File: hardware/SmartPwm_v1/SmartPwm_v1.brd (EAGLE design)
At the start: 100 x 80 mm, 22 parts, among them IC1 7805T, J1 ESP32-PICO-KIT, Q1 IRF3704-H, Q2 IRF3704-H, Q3 IRF3704-H, Q4 IRF3704-H, U1 ICL7667CPAZ, U2 ICL7667CPAZ

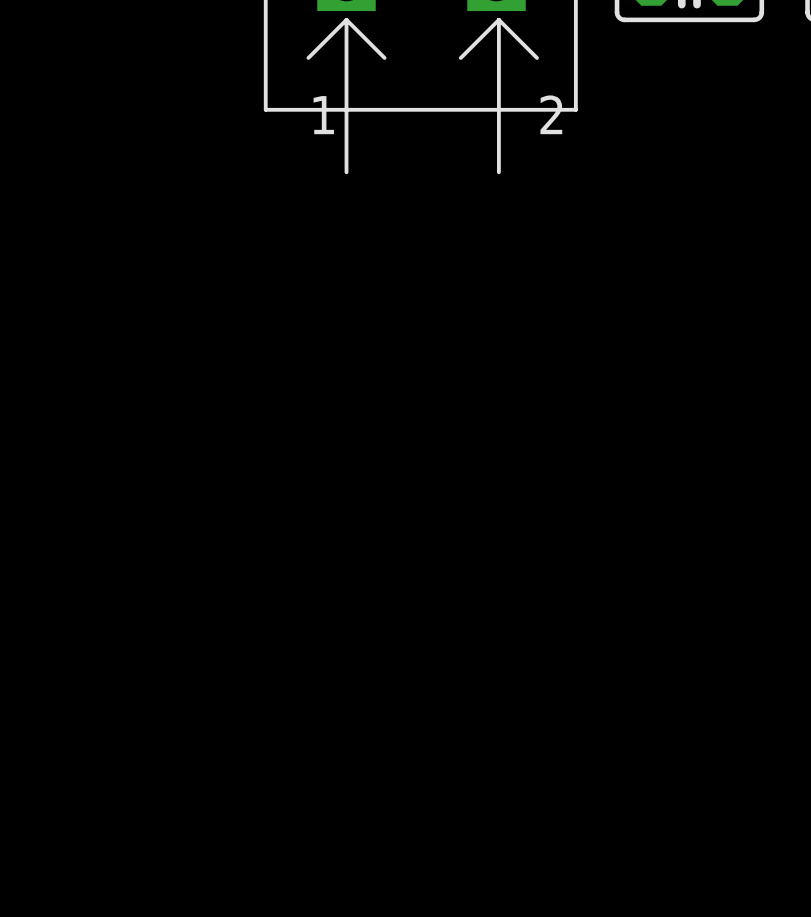
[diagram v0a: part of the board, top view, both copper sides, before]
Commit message: Add header for IIC LCD display and add dht11 temp sensor
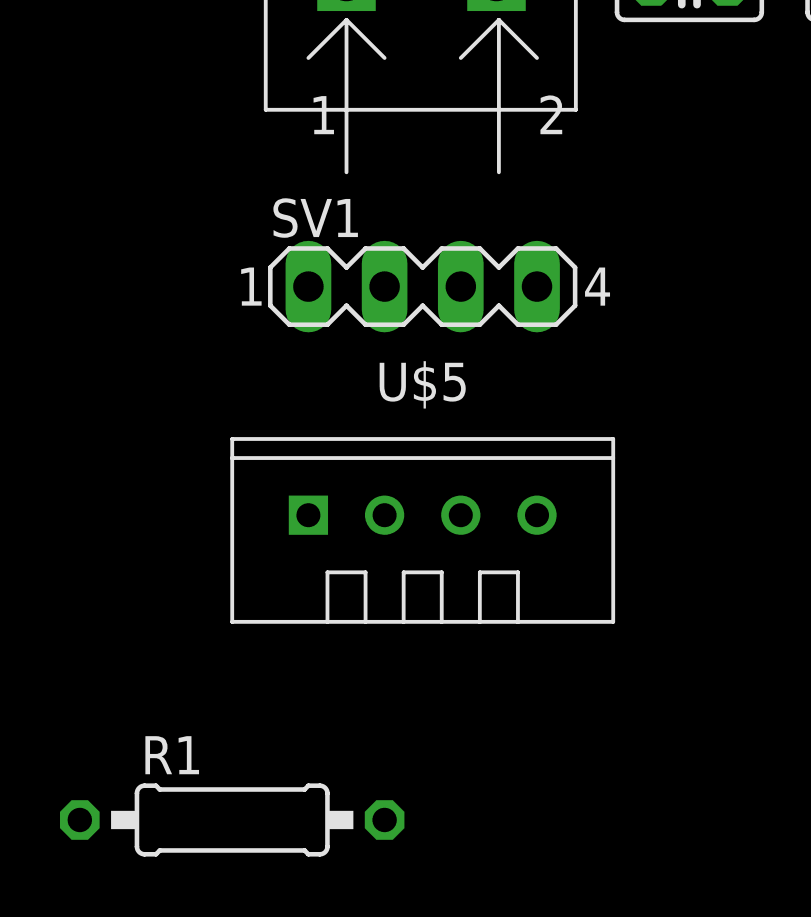
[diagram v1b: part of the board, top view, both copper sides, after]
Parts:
- added R1: (no value), rcl:0207/10
- added SV1: (no value), con-lstb:MA04-1
- added U$5: TEMP-HUM-SENSOR-DHT11, diy-modules:TEMP-HUM-SENSOR-DHT11
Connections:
- new net SCL: J1.J2_5, SV1.4
- new net SDA: J1.J2_4, SV1.3
- new net TDAT: J1.J2_8, R1.2, U$5.2
- net GND: now also SV1.1, U$5.4
- net VCC: now also SV1.2
- net VEE: now also R1.1, U$5.1
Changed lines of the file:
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@@
 <layer number="97" name="Info" color="7" fill="1" visible="no" active="no"/>
 <layer number="98" name="Guide" color="6" fill="1" visible="no" active="no"/>
+<layer number="101" name="Hidden" color="15" fill="1" visible="yes" active="yes"/>
+<layer number="102" name="Changes" color="12" fill="1" visible="yes" active="yes"/>
 </layers>
 <board>
@@
 <attribute name="VALUE" x="-41.021" y="-52.324" size="1.27" layer="27" ratio="10"/>
 </element>
+<element name="SV1" library="con-lstb" library_urn="urn:adsk.eagle:library:162" package="MA04-1" package3d_urn="urn:adsk.eagle:package:8337/1" value="" x="-64.77" y="-59.69" smashed="yes">
+<attribute name="MF" value="" x="-64.77" y="-59.69" size="1.778" layer="27" display="off"/>
+<attribute name="MPN" value="" x="-64.77" y="-59.69" size="1.778" layer="27" display="off"/>
+<attribute name="NAME" x="-69.85" y="-58.039" size="1.27" layer="25" ratio="10"/>
+<attribute name="OC_FARNELL" value="unknown" x="-64.77" y="-59.69" size="1.778" layer="27" display="off"/>
+<attribute name="OC_NEWARK" value="unknown" x="-64.77" y="-59.69" size="1.778" layer="27" display="off"/>
+<attribute name="POPULARITY" value="41" x="-64.77" y="-59.69" size="1.778" layer="27" display="off"/>
+<attribute name="VALUE" x="-64.135" y="-58.039" size="1.27" layer="27" ratio="10"/>
+</element>
+<element name="U$5" library="diy-modules" package="TEMP-HUM-SENSOR-DHT11" value="TEMP-HUM-SENSOR-DHT11" x="-64.77" y="-67.31" smashed="yes">
+<attribute name="NAME" x="-64.77" y="-63.5" size="1.27" layer="25" align="bottom-center"/>
+<attribute name="VALUE" x="-64.77" y="-72.39" size="1.27" layer="27" align="top-center"/>
+</element>
+<element name="R1" library="rcl" library_urn="urn:adsk.eagle:library:334" package="0207/10" package3d_urn="urn:adsk.eagle:package:23491/2" value="" x="-71.12" y="-77.47" smashed="yes">
+<attribute name="NAME" x="-74.168" y="-75.946" size="1.27" layer="25" ratio="10"/>
+<attribute name="POPULARITY" value="36" x="-71.12" y="-77.47" size="1.778" layer="27" display="off"/>
+<attribute name="SPICEPREFIX" value="R" x="-71.12" y="-77.47" size="1.778" layer="27" display="off"/>
+<attribute name="VALUE" x="-73.3806" y="-78.105" size="1.27" layer="27" ratio="10"/>
+</element>
 </elements>
 <signals>
@@
 <contactref element="C7" pad="2"/>
 <contactref element="C8" pad="2"/>
+<contactref element="SV1" pad="1"/>
+<contactref element="U$5" pad="4"/>
+<wire x1="-60.96" y1="-67.31" x2="-68.58" y2="-59.69" width="0" layer="19" extent="1-1"/>
+<wire x1="-54.61" y1="-49.53" x2="-68.58" y2="-59.69" width="0" layer="19" extent="1-1"/>
+<wire x1="-48.26" y1="-49.53" x2="-54.61" y2="-49.53" width="0" layer="19" extent="1-1"/>
+<wire x1="-69.85" y1="-36.83" x2="-54.61" y2="-49.53" width="0" layer="19" extent="1-1"/>
 <wire x1="-63.5" y1="-22.86" x2="-69.85" y2="-36.83" width="0" layer="19" extent="1-1"/>
 <wire x1="-48.26" y1="-22.86" x2="-63.5" y2="-22.86" width="0" layer="19" extent="1-1"/>
-<wire x1="-54.61" y1="-49.53" x2="-69.85" y2="-36.83" width="0" layer="19" extent="1-1"/>
-<wire x1="-48.26" y1="-49.53" x2="-54.61" y2="-49.53" width="0" layer="19" extent="1-1"/>
 <wire x1="-17.78" y1="6.35" x2="-48.26" y2="-22.86" width="0" layer="19" extent="1-1"/>
 <wire x1="-17.78" y1="24.13" x2="-17.78" y2="6.35" width="0" layer="19" extent="1-1"/>
@@
 <contactref element="C1" pad="1"/>
 <contactref element="J1" pad="J3_20"/>
-<wire x1="-49.53" y1="31.75" x2="-16.51" y2="77.47" width="0" layer="19" extent="1-1"/>
-<wire x1="-15.24" y1="6.35" x2="-49.53" y2="31.75" width="0" layer="19" extent="1-1"/>
+<contactref element="SV1" pad="2"/>
+<wire x1="-15.24" y1="6.35" x2="-66.04" y2="-59.69" width="0" layer="19" extent="1-1"/>
+<wire x1="-49.53" y1="31.75" x2="-15.24" y2="6.35" width="0" layer="19" extent="1-1"/>
+<wire x1="-16.51" y1="77.47" x2="-49.53" y2="31.75" width="0" layer="19" extent="1-1"/>
 </signal>
 <signal name="VDD">
@@
 <contactref element="J1" pad="J2_20"/>
 <contactref element="J1" pad="J3_18"/>
+<contactref element="U$5" pad="1"/>
+<contactref element="R1" pad="1"/>
+<wire x1="-68.58" y1="-67.31" x2="-76.2" y2="-77.47" width="0" layer="19" extent="1-1"/>
+<wire x1="-20.32" y1="6.35" x2="-68.58" y2="-67.31" width="0" layer="19" extent="1-1"/>
 <wire x1="-15.24" y1="24.13" x2="-20.32" y2="6.35" width="0" layer="19" extent="1-1"/>
 </signal>
@@
 <wire x1="-66.04" y1="-22.86" x2="-40.720009375" y2="-29.21" width="0" layer="19" extent="1-1"/>
 </signal>
+<signal name="SCL">
+<contactref element="SV1" pad="4"/>
+<contactref element="J1" pad="J2_5"/>
+<wire x1="-53.34" y1="24.13" x2="-60.96" y2="-59.69" width="0" layer="19" extent="1-1"/>
+</signal>
+<signal name="SDA">
+<contactref element="SV1" pad="3"/>
+<contactref element="J1" pad="J2_4"/>
+<wire x1="-55.88" y1="24.13" x2="-63.5" y2="-59.69" width="0" layer="19" extent="1-1"/>
+</signal>
+<signal name="TDAT">
+<contactref element="U$5" pad="2"/>
+<contactref element="R1" pad="2"/>
+<contactref element="J1" pad="J2_8"/>
+<wire x1="-66.04" y1="-67.31" x2="-66.04" y2="-77.47" width="0" layer="19" extent="1-1"/>
+<wire x1="-45.72" y1="24.13" x2="-66.04" y2="-67.31" width="0" layer="19" extent="1-1"/>
+</signal>
 </signals>

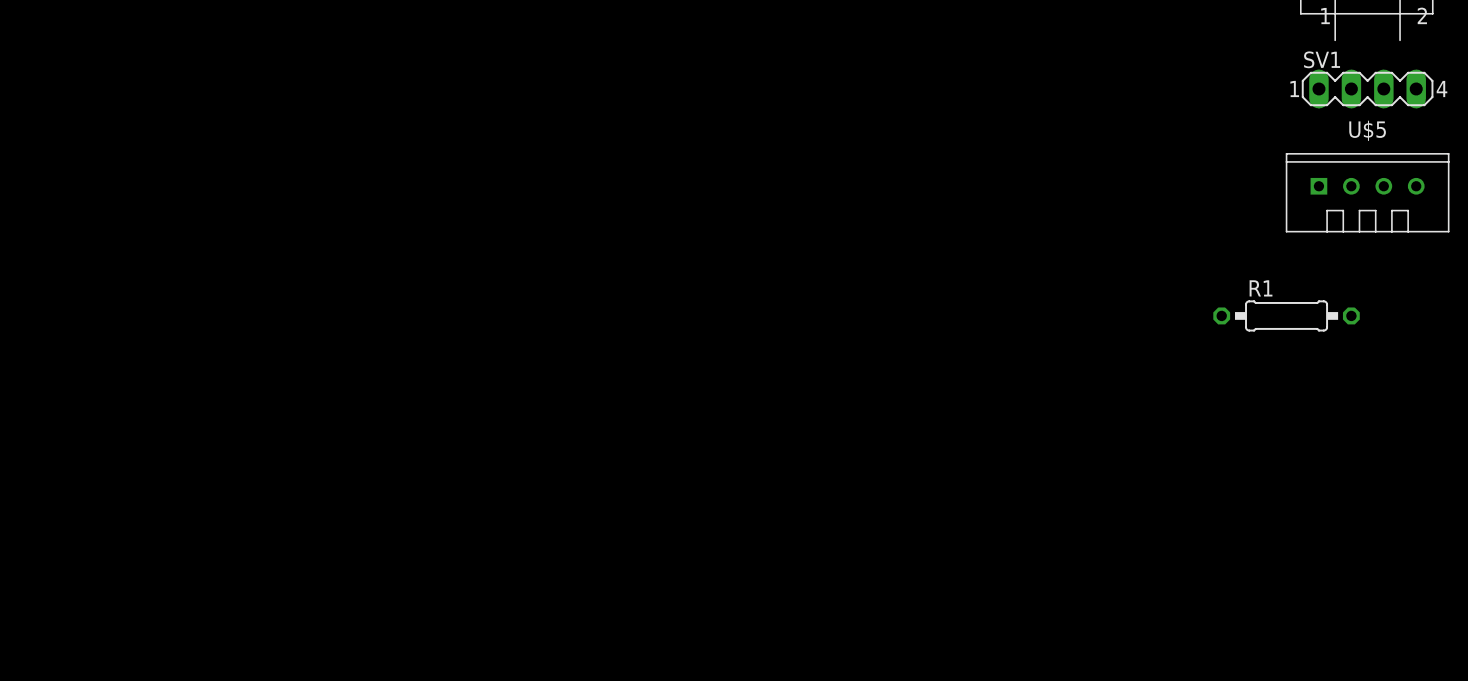
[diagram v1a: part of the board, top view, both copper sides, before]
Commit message: add knobs to schematic, rearrange ios, select lcd and add to docs
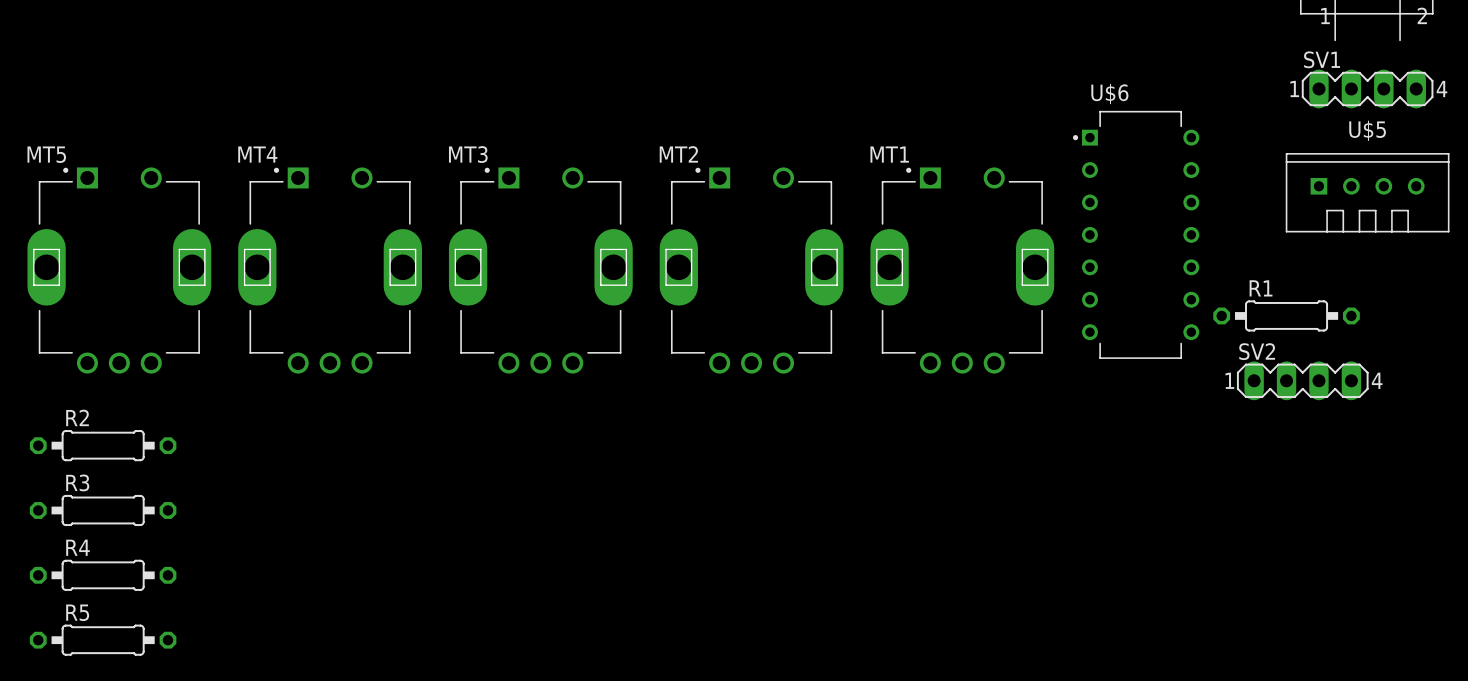
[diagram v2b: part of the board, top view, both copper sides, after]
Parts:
- added MT1, MT2, MT3, MT4, MT5: PEC11R-4215F-S0024, PEC11R-4215F-S0024:XDCR_PEC11R-4215F-S0024
- added R2: 10M, rcl:0207/10
- added R3: 1M, rcl:0207/10
- added R4, R5: 10K, rcl:0207/10
- added SV2: (no value), con-lstb:MA04-1
- added U$6: 74AHTC125, DIP794W45P254L1969H508Q14:DIP794W45P254L1969H508Q14
- C10, C5, C6, C9: value (none) -> 10uf
- R1: value (none) -> 10K
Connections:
- new net K1_A: J1.J3_15, MT1.A
- new net K1_B: J1.J2_9, MT1.B
- new net K1_S: J1.J3_17, MT1.2
- new net K2_A: J1.J3_7, MT2.A
- new net K2_B: J1.J2_10, MT2.B
- new net K2_S: J1.J3_16, MT2.2
- new net K3_A: J1.J3_8, MT3.A
- new net K3_B: J1.J2_11, MT3.B
- new net K3_S: J1.J3_10, MT3.2
- new net K4_A: J1.J2_14, MT4.A
- new net K4_B: MT4.B
- new net K4_S: J1.J2_15, MT4.2
- new net K5_A: J1.J3_9, MT5.A
- new net K5_B: J1.J3_6, MT5.B
- new net K5_S: J1.J2_17, MT5.2
- new net LDAT3V3: J1.J2_6, U$6.2
- new net LDAT5V: SV2.2, SV2.3, U$6.3
- new net VDIV: J1.J2_16, R2.1, R3.2
- net GND: now also MT1.1, MT1.COM, MT1.S1, MT1.S2, MT2.1, MT2.COM, MT2.S1, MT2.S2, MT3.1, MT3.COM, MT3.S1, MT3.S2, MT4.1, MT4.COM, MT4.S1, MT4.S2, MT5.1, MT5.COM, MT5.S1, MT5.S2, R3.1, SV2.1, U$6.1, U$6.5, U$6.7, U$6.9
- net SCL: now also R4.2
- net SDA: now also R5.2
- net VCC: now also U$6.10, U$6.12, U$6.13, U$6.14, U$6.4; no longer SV1.2
- net VDD: now also R2.2, SV2.4
- net VEE: now also R4.1, R5.1, SV1.2

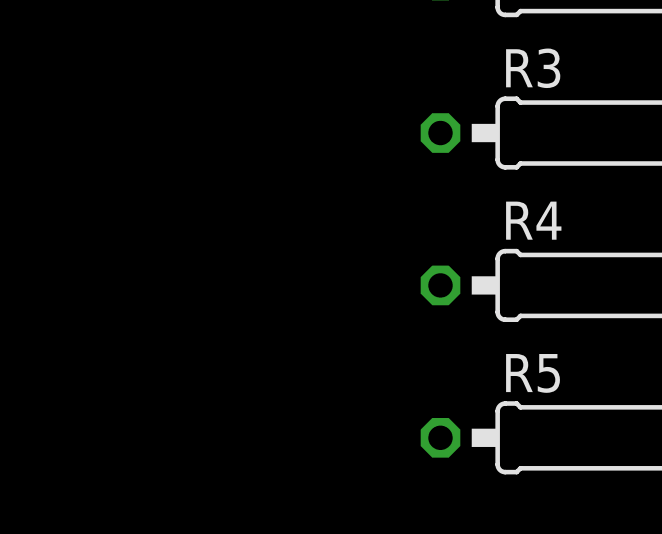
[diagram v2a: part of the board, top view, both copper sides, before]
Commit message: add optional grove connector for IIC bus
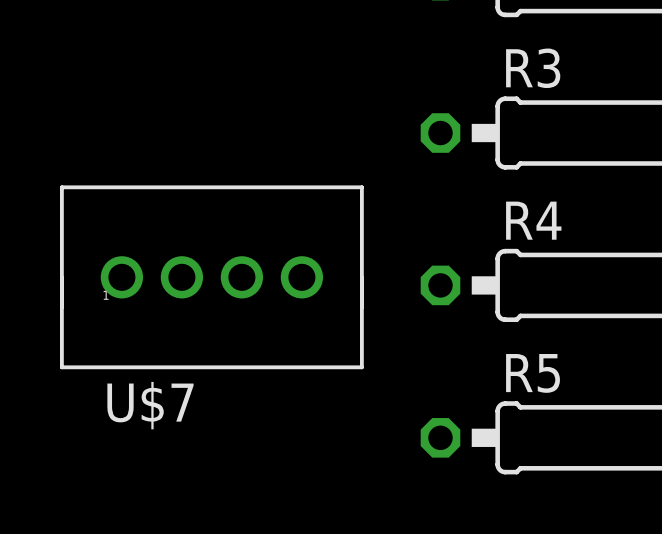
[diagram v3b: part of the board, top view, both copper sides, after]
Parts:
- added U$7: 110990030, seeedgrove:110990030-VERTICAL-GROVE-CONNECTOR
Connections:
- net GND: now also U$7.4
- net SCL: now also U$7.1
- net SDA: now also U$7.2
- net VEE: now also U$7.3
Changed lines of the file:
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@@
 <attribute name="VALUE" x="-166.0906" y="-103.505" size="1.27" layer="27" ratio="10"/>
+</element>
+<element name="U$7" library="seeedgrove" package="110990030-VERTICAL-GROVE-CONNECTOR" value="110990030" x="-176.53" y="-96.52" smashed="yes">
+<attribute name="NAME" x="-180.15" y="-102.33" size="1.27" layer="25"/>
+<attribute name="VALUE" x="-180.15" y="-93.98" size="1.27" layer="27"/>
 </element>
 </elements>
@@
 <contactref element="MT5" pad="1"/>
 <contactref element="R3" pad="1"/>
+<contactref element="U$7" pad="4"/>
 <wire x1="-165.06" y1="-66.66" x2="-168.26" y2="-73.66" width="0" layer="19" extent="1-1"/>
 <wire x1="-162.56" y1="-81.16" x2="-168.26" y2="-73.66" width="0" layer="19" extent="1-1"/>
@@
 <wire x1="-86.52" y1="-63.5" x2="-86.52" y2="-73.66" width="0" layer="19" extent="1-1"/>
 <wire x1="-168.91" y1="-92.71" x2="-162.56" y2="-81.16" width="0" layer="19" extent="1-1"/>
+<wire x1="-173.53" y1="-97.52" x2="-168.91" y2="-92.71" width="0" layer="19" extent="1-1"/>
 <wire x1="-68.58" y1="-59.69" x2="-86.52" y2="-63.5" width="0" layer="19" extent="1-1"/>
 <wire x1="-60.96" y1="-67.31" x2="-68.58" y2="-59.69" width="0" layer="19" extent="1-1"/>
@@
 <contactref element="R4" pad="1"/>
 <contactref element="R5" pad="1"/>
+<contactref element="U$7" pad="3"/>
 <wire x1="-68.58" y1="-67.31" x2="-76.2" y2="-77.47" width="0" layer="19" extent="1-1"/>
 <wire x1="-66.04" y1="-59.69" x2="-68.58" y2="-67.31" width="0" layer="19" extent="1-1"/>
@@
 <wire x1="-168.91" y1="-97.79" x2="-76.2" y2="-77.47" width="0" layer="19" extent="1-1"/>
 <wire x1="-168.91" y1="-102.87" x2="-168.91" y2="-97.79" width="0" layer="19" extent="1-1"/>
+<wire x1="-175.53" y1="-97.52" x2="-168.91" y2="-97.79" width="0" layer="19" extent="1-1"/>
 </signal>
 <signal name="CTRL4">
@@
 <contactref element="J1" pad="J2_5"/>
 <contactref element="R4" pad="2"/>
+<contactref element="U$7" pad="1"/>
 <wire x1="-53.34" y1="24.13" x2="-60.96" y2="-59.69" width="0" layer="19" extent="1-1"/>
 <wire x1="-158.75" y1="-97.79" x2="-60.96" y2="-59.69" width="0" layer="19" extent="1-1"/>
+<wire x1="-179.53" y1="-97.52" x2="-158.75" y2="-97.79" width="0" layer="19" extent="1-1"/>
 </signal>
 <signal name="SDA">
@@
 <contactref element="J1" pad="J2_4"/>
 <contactref element="R5" pad="2"/>
+<contactref element="U$7" pad="2"/>
 <wire x1="-55.88" y1="24.13" x2="-63.5" y2="-59.69" width="0" layer="19" extent="1-1"/>
 <wire x1="-158.75" y1="-102.87" x2="-63.5" y2="-59.69" width="0" layer="19" extent="1-1"/>
+<wire x1="-177.53" y1="-97.52" x2="-158.75" y2="-102.87" width="0" layer="19" extent="1-1"/>
 </signal>
 <signal name="TDAT">

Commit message: swap out components for smt options, research jst 4 pin for leds
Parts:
- removed C2: .33uf, capacitor-wima:C2.5-2
- removed R1, R4, R5: 10K, rcl:0207/10
- removed R2: 10M, rcl:0207/10
- removed R3: 1M, rcl:0207/10
- removed U2: ICL7667CPAZ, ICL7667CPAZ:DIP254P762X533-8
- added C11: AVX_TPSA475K020R1800AVX_TPSA475K020R1800_0_0, AVX - TPSA475K020R1800:AVX_TPSA475K020R1800_0
- added C12: .1uf, rcl:C0805
- added R10: 1M, rcl:R0805
- added R6, R8: 10K, rcl:R0805
- added R7: 10k, rcl:R0805
- added R9: 10M, rcl:R0805
- added U$8: TB002-500-P02, mylib:TB002-500-P02
- added U3: ICL7667CBAZA, ICL7667CBAZA:SOIC127P600X175-8N
- C1, C8: value .1uf -> 10uf; device capacitor-wima:C2.5-2 -> rcl:C0805
- C10: value 10uf -> AVX_TPSA475K020R1800AVX_TPSA475K020R1800_0_0; device capacitor-wima:C2.5-2 -> AVX - TPSA475K020R1800:AVX_TPSA475K020R1800_0
- C3: value 4.7uf -> .33uf; device capacitor-wima:C2.5-2 -> rcl:C0805
- C4, C5, C6, C9: device capacitor-wima:C2.5-2 -> rcl:C0805
- C7: value 4.7uf -> .1uf; device capacitor-wima:C2.5-2 -> rcl:C0805
- U$6: value 74AHTC125 -> 74AHTC125NSR; device DIP794W45P254L1969H508Q14:DIP794W45P254L1969H508Q14 -> DIP794W45P254L1969H508Q14:SOP127P780X200-14N
- U1: value ICL7667CPAZ -> ICL7667CBAZA; device ICL7667CPAZ:DIP254P762X533-8 -> ICL7667CBAZA:SOIC127P600X175-8N
- moved C1 349.9 mm to (-201.9, -218.4)
- moved U1 305.1 mm to (-190.5, -196.8)
- moved C4 284.6 mm to (-179.1, -158.8)
- moved C6 252.8 mm to (-179.1, -129.5)
- moved C5 250.7 mm to (-179.1, -123.2)
- moved C3 236.3 mm to (-179.1, -152.4)
- moved U$6 170.7 mm to (-199.4, -195.6)
- moved C10 169.5 mm to (-177.8, -147.3)
- moved C9 159.9 mm to (-179.1, -135.9)
- moved C8 146.0 mm to (-179.1, -116.8)
- moved C7 137.4 mm to (-179.1, -110.5)
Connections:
- net CTRL1: now also U3.2; no longer U1.2
- net CTRL2: now also U3.4; no longer U1.4
- net CTRL3: now also U1.2; no longer U2.2
- net CTRL4: now also U1.4; no longer U2.4
- net GATE1: now also U3.7; no longer U1.7
- net GATE2: now also U3.5; no longer U1.5
- net GATE3: now also U1.7; no longer U2.7
- net GATE4: now also U1.5; no longer U2.5
- net GND: now also C10.1, C11.1, C12.2, R10.2, U$8.P$2, U3.3; no longer C2.2, C8.2, R3.1, U2.3
- net LOAD_RET1: now also C9.2; no longer C5.2
- net LOAD_RET3: now also C8.2; no longer C9.2
- net LOAD_RET4: now also C5.2; no longer C10.2
- net SCL: now also R7.2; no longer R4.2
- net SDA: now also R8.2; no longer R5.2
- net TDAT: now also R6.2; no longer R1.2
- net VCC: now also C4.1; no longer C1.1
- net VDD: now also C1.1, C10.2, C11.2, C12.1, R9.1, U$8.P$1, U3.6; no longer C10.1, C2.1, C4.1, R2.2, U2.6
- net VDIV: now also R10.1, R9.2; no longer R2.1, R3.2
- net VEE: now also R6.1, R7.1, R8.1; no longer R1.1, R4.1, R5.1

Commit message: add 3 more led strips, time to start layout!
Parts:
- added SV3, SV4, SV5: (no value), con-lstb:MA04-1
- R10: value 1M -> 5K
- R9: value 10M -> 25K
- moved Q3 183.1 mm to (94.0, 72.4)
- moved Q1 121.5 mm to (96.5, 15.2)
- moved Q4 112.8 mm to (15.2, 74.9)
- moved J1 99.3 mm to (53.3, 50.8)
- moved Q2 58.3 mm to (16.5, 17.8)
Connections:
- net GND: now also SV3.1, SV4.1, SV5.1
- net LDAT5V: now also SV3.2, SV3.3, SV4.2, SV4.3, SV5.2, SV5.3
- net VDD: now also SV3.4, SV4.4, SV5.4
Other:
- board size 100 x 80 mm -> 154.6 x 198.1 mm
